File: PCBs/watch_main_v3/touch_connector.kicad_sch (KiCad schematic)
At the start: 1 part, among them J601 AXG110144A

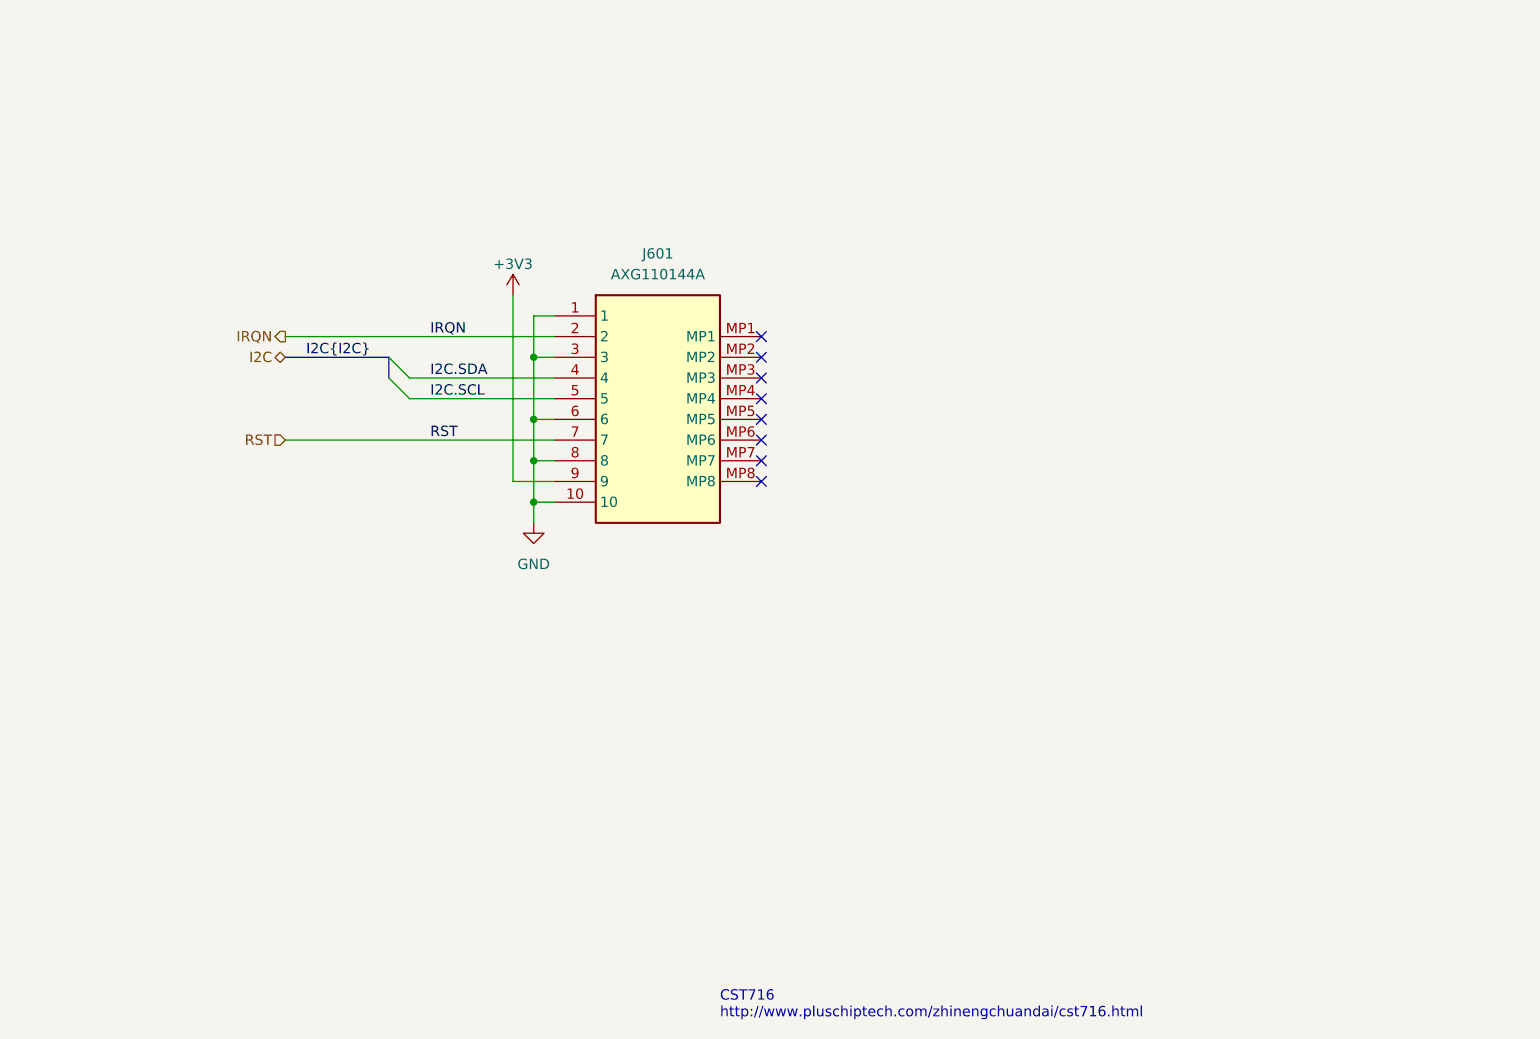
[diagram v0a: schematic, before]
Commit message: Created touch connector footprint
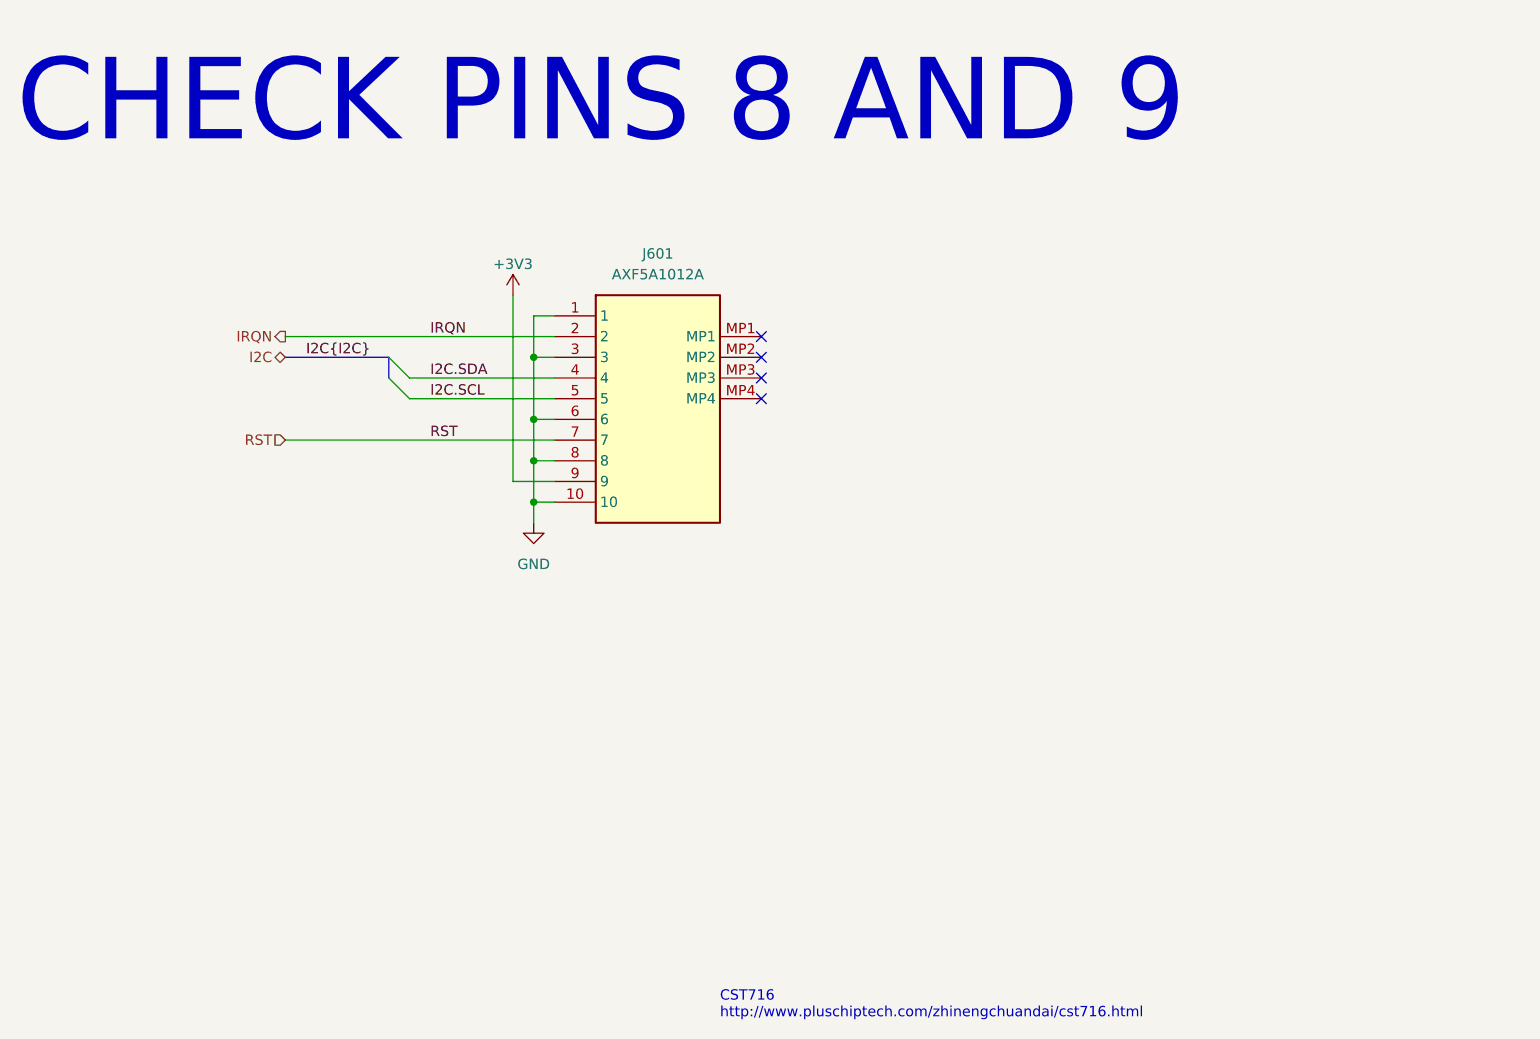
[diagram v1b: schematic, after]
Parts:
- removed J601: AXG110144A, watch_footprints:AXG110144A, symbol AXG110144A:AXG110144A
- added J601: AXF5A1012A, watch_footprints:AXF5A1012A, symbol watch_symbols_lib:AXF5A1012A
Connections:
- net +3V3: now also J601.9
- net GND: now also J601.1, J601.10, J601.3, J601.6, J601.8
- net I2C.SCL: now also J601.5
- net I2C.SDA: now also J601.4
- net IRQN: now also J601.2
- net RST: now also J601.7
- no-connect marks 8 -> 4
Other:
- note added: "CHECK PINS 8 AND 9"
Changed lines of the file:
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@@
   (junction (at 132.08 88.9) (diameter 0) (color 0 0 0 0)
   )
-  (no_connect (at 160.02 91.44))
   (no_connect (at 160.02 78.74))
-  (no_connect (at 160.02 88.9))
   (no_connect (at 160.02 81.28))
-  (no_connect (at 160.02 83.82))
-  (no_connect (at 160.02 86.36))
   (no_connect (at 160.02 73.66))
   (no_connect (at 160.02 76.2))
@@
     (effects (font (size 1.27 1.27)) (justify left bottom))
   )
+  (text "CHECK PINS 8 AND 9" (at 68.58 50.8 0)
+    (effects (font (size 10 10)) (justify left bottom))
+  )
   (label "I2C{I2C}" (at 104.14 76.2 0) (fields_autoplaced)
     (effects (font (size 1.27 1.27)) (justify left bottom))
@@
     )
   )
-  (symbol (lib_id "AXG110144A:AXG110144A") (at 147.32 81.28 0) (unit 1)
-    (in_bom yes) (on_board yes) (dnp no)
-    (property "Reference" "J601" (at 147.32 63.5 0)
-      (effects (font (size 1.27 1.27)))
-    )
-    (property "Value" "AXG110144A" (at 147.32 66.04 0)
-      (effects (font (size 1.27 1.27)))
-    )
-    (property "Footprint" "watch_footprints:AXG110144A" (at 166.37 176.2 0)
-      (effects (font (size 1.27 1.27)) (justify left top) hide)
-    )
-    (property "Datasheet" "https://www3.panasonic.biz/ac/ae/search_num/index.jsp?c=detail&part_no=AXG110144&large_g_cd=1&medium_g_cd=12&small_g_cd=122&series_cd=3192" (at 166.37 276.2 0)
-      (effects (font (size 1.27 1.27)) (justify left top) hide)
-    )
-    (property "Height" "0.79" (at 166.37 476.2 0)
-      (effects (font (size 1.27 1.27)) (justify left top) hide)
-    )
-    (property "Mouser Part Number" "N/A" (at 166.37 576.2 0)
-      (effects (font (size 1.27 1.27)) (justify left top) hide)
-    )
-    (property "Mouser Price/Stock" "http://www.mouser.com/Search/ProductDetail.aspx?qs=aVrSikiHukR%252bjc9q3Ez0%2fQ%3d%3d" (at 166.37 676.2 0)
-      (effects (font (size 1.27 1.27)) (justify left top) hide)
-    )
-    (property "Manufacturer_Name" "Panasonic" (at 166.37 776.2 0)
-      (effects (font (size 1.27 1.27)) (justify left top) hide)
-    )
-    (property "Manufacturer_Part_Number" "AXG110144A" (at 166.37 876.2 0)
-      (effects (font (size 1.27 1.27)) (justify left top) hide)
-    )
-    (pin "1")
-    (pin "10")
-    (pin "2")
-    (pin "3")
-    (pin "4")
-    (pin "5")
-    (pin "6")
-    (pin "7")
-    (pin "8")
-    (pin "9")
-    (pin "MP1")
-    (pin "MP2")
-    (pin "MP3")
-    (pin "MP4")
-    (pin "MP5")
-    (pin "MP6")
-    (pin "MP7")
-    (pin "MP8")
-    (instances
-      (project "watch_main"
-        (path "/b008648a-c7cf-4e14-8a0a-b9314d757b4a/33389a00-643f-4d0e-bdc2-cdeb49d6ab4d"
-          (reference "J601") (unit 1)
-        )
-      )
-    )
-  )
   (symbol (lib_id "power:GND") (at 132.08 96.52 0) (unit 1)
     (in_bom yes) (on_board yes) (dnp no) (fields_autoplaced)
@@
         )
       )
+    )
+  )
+  (symbol (lib_id "watch_symbols_lib:AXF5A1012A") (at 147.32 81.28 0) (unit 1)
+    (in_bom yes) (on_board yes) (dnp no) (fields_autoplaced)
+    (property "Reference" "J601" (at 147.32 63.5 0)
+      (effects (font (size 1.27 1.27)))
+    )
+    (property "Value" "AXF5A1012A" (at 147.32 66.04 0)
+      (effects (font (size 1.27 1.27)))
+    )
+    (property "Footprint" "watch_footprints:AXF5A1012A" (at 166.37 176.2 0)
+      (effects (font (size 1.27 1.27)) (justify left top) hide)
+    )
+    (property "Datasheet" "https://www3.panasonic.biz/ac/e_download/control/connector/battery/catalog/con_eng_a35p.pdf" (at 166.37 276.2 0)
+      (effects (font (size 1.27 1.27)) (justify left top) hide)
+    )
+    (property "Height" "" (at 166.37 476.2 0)
+      (effects (font (size 1.27 1.27)) (justify left top) hide)
+    )
+    (property "Mouser Part Number" "" (at 166.37 576.2 0)
+      (effects (font (size 1.27 1.27)) (justify left top) hide)
+    )
+    (property "Mouser Price/Stock" "" (at 166.37 676.2 0)
+      (effects (font (size 1.27 1.27)) (justify left top) hide)
+    )
+    (property "Manufacturer_Name" "" (at 166.37 776.2 0)
+      (effects (font (size 1.27 1.27)) (justify left top) hide)
+    )
+    (property "Manufacturer_Part_Number" "" (at 166.37 876.2 0)
+      (effects (font (size 1.27 1.27)) (justify left top) hide)
+    )
+    (pin "MP1")
+    (pin "5")
+    (pin "MP2")
+    (pin "3")
+    (pin "6")
+    (pin "2")
+    (pin "7")
+    (pin "1")
+    (pin "4")
+    (pin "MP4")
+    (pin "10")
+    (pin "MP3")
+    (pin "9")
+    (pin "8")
+    (instances
+      (project "watch_main"
+        (path "/b008648a-c7cf-4e14-8a0a-b9314d757b4a/33389a00-643f-4d0e-bdc2-cdeb49d6ab4d"
+          (reference "J601") (unit 1)
+        )
+      )

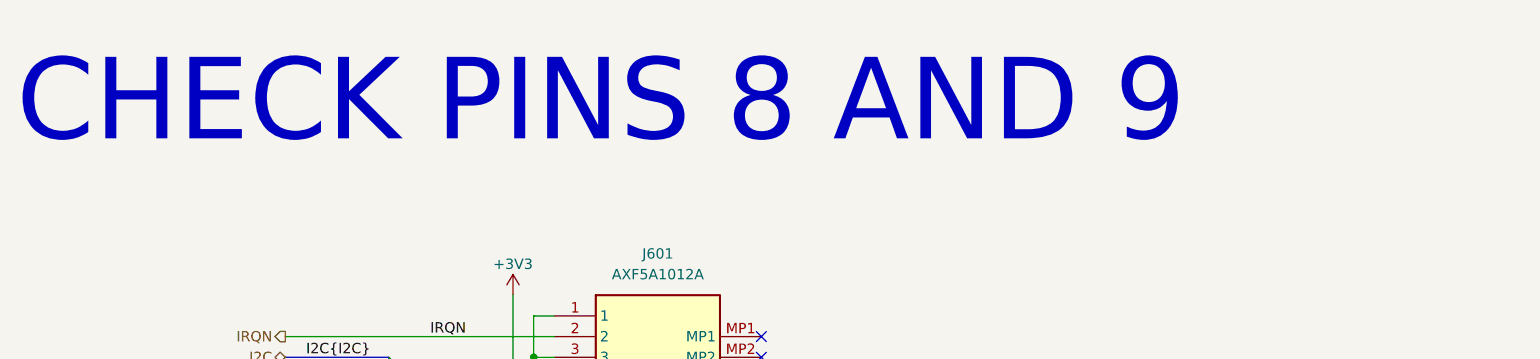
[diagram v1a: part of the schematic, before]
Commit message: Swapped in new touch connector footprint
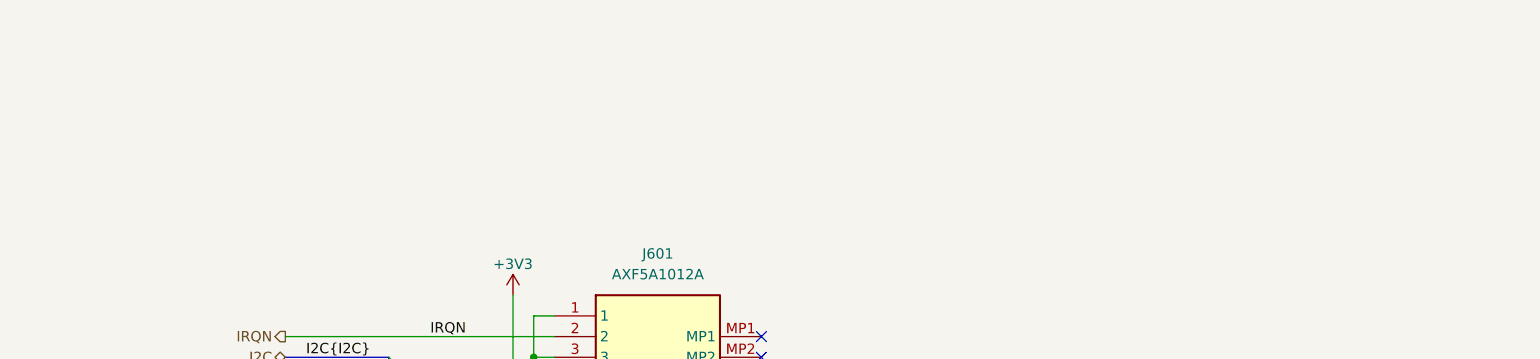
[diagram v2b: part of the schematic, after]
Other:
- note removed: "CHECK PINS 8 AND 9"
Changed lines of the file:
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@@
     (effects (font (size 1.27 1.27)) (justify left bottom))
-  )
-  (text "CHECK PINS 8 AND 9" (at 68.58 50.8 0)
-    (effects (font (size 10 10)) (justify left bottom))
   )
   (label "I2C{I2C}" (at 104.14 76.2 0) (fields_autoplaced)

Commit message: PCB V3 progress
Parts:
- added R601: 100k, Resistor_SMD:R_0402_1005Metric, symbol Device:R_Small
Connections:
- net +3V3: now also R601.1
- net RST: now also R601.2
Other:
- note added: "RST Must be open drain"
